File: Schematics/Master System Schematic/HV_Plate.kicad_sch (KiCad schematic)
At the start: 14 parts, among them K5 AIR-: GX14, K6 PCharge: P105BDA, K7 AIR+: GX14, K8 DCharge: PNC113, U7 OrionCurrentSens

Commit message: ESF-2 2023 Updates (#136)
* Moved shutdown loop & TSMPs

* Moved Dashboard/Footwellbox

* Deleted SSOKs

* More stuff

* Charger and battbox stuff

* Added battbox fans

* Updated sheet sizing

* Flipped MC

 to make powertrain ordering better

* Updated HV plate

* IDrk

* Better topsheet labels

* Segment Layer updates

Adding shepherd

* LV Plate update

* Partial work on accumulator container sheet

To be continued

* Finish accumulator

* Footwell updates

* Removing old files

* Added Wheel

* Top sheet budge

* Renumbered pages

* Shutdown Summary Updates

* Missed some TSV color

* Export shutdown summary

* Deleted more old files

* Added TSAL17

* Added TS-GLV17

* Added Wheel17

* Other NER lib cleanup

* Annotations

* More annotate and export

* Moved PDF

* Reexport master schem

* Cleaning out old shutdown summary files

* MATLAB!

For precharge and discharge plotting

* Changed label alignment

* Updated dashboard name

* Updated for LFP board and bigger top sheet

* backup

* Changed breaker to fuse in Shutdown Simmary

* Finished traces

* Oops forgot to merge
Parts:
- added F906: DCDC Fuse+: 5A, symbol Device:Fuse
- added F907: DCDC Fuse-: 5A, symbol Device:Fuse
- K901: renamed from K5; value AIR-: GX14 -> AIR-: GV24
- K902: renamed from K6; value PCharge: P105BDA -> PCharge: 2-1904058-5
- K903: renamed from K7; value AIR+: GX14 -> AIR+: GV24
- K904: renamed from K8; value DCharge: PNC113 -> DCharge: CPC1135N
- R901: renamed from R8; value PCharge: 600R -> PCharge: 1K
- R902: renamed from R9; value DCharge: 3.3K -> DCharge: 5K
- renumbered F190 to F901, F191 to F902, F192 to F903, F193 to F904, F194 to F905, R10 to R903, R11 to R904, U7 to U901
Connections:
- net AIR-_SigL is gone; now on net RlyCtrlGND: K901.6
- net DCharge_SigL is gone; now on net RlyCtrlGND: K904.5
- net PCharge_SigL is gone; now on net RlyCtrlGND: K902.6
- net TS+: now also F906.1
- net TS-: now also F907.1
- net AIR+_SigL renamed RlyCtrlGND
- new net DCDC_TS+: F906.2
- new net DCDC_TS-: F907.2
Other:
- note added: "SEE ALTIUM SCHEMATIC FOR FINAL IMPLEMENTATION"
- note removed: "20AWG"

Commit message: Revert "ESF-2 2023 Updates (#136)"
This reverts commit dbac7da28cdaad5f36fde89af32aad76a0b85ea3.
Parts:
- removed F906: DCDC Fuse+: 5A, symbol Device:Fuse
- removed F907: DCDC Fuse-: 5A, symbol Device:Fuse
- K5: renamed from K901; value AIR-: GV24 -> AIR-: GX14
- K6: renamed from K902; value PCharge: 2-1904058-5 -> PCharge: P105BDA
- K7: renamed from K903; value AIR+: GV24 -> AIR+: GX14
- K8: renamed from K904; value DCharge: CPC1135N -> DCharge: PNC113
- R8: renamed from R901; value PCharge: 1K -> PCharge: 600R
- R9: renamed from R902; value DCharge: 5K -> DCharge: 3.3K
- renumbered F901 to F190, F902 to F191, F903 to F192, F904 to F193, F905 to F194, R903 to R10, R904 to R11, U901 to U7
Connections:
- removed net RlyCtrlGND: K5.6, K6.6, K7.6, K8.5
- new net AIR+_SigL: K7.6
- new net AIR-_SigL: K5.6
- new net DCharge_SigL: K8.5
- new net PCharge_SigL: K6.6
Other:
- note added: "20AWG"
- note removed: "SEE ALTIUM SCHEMATIC FOR FINAL IMPLEMENTATION"

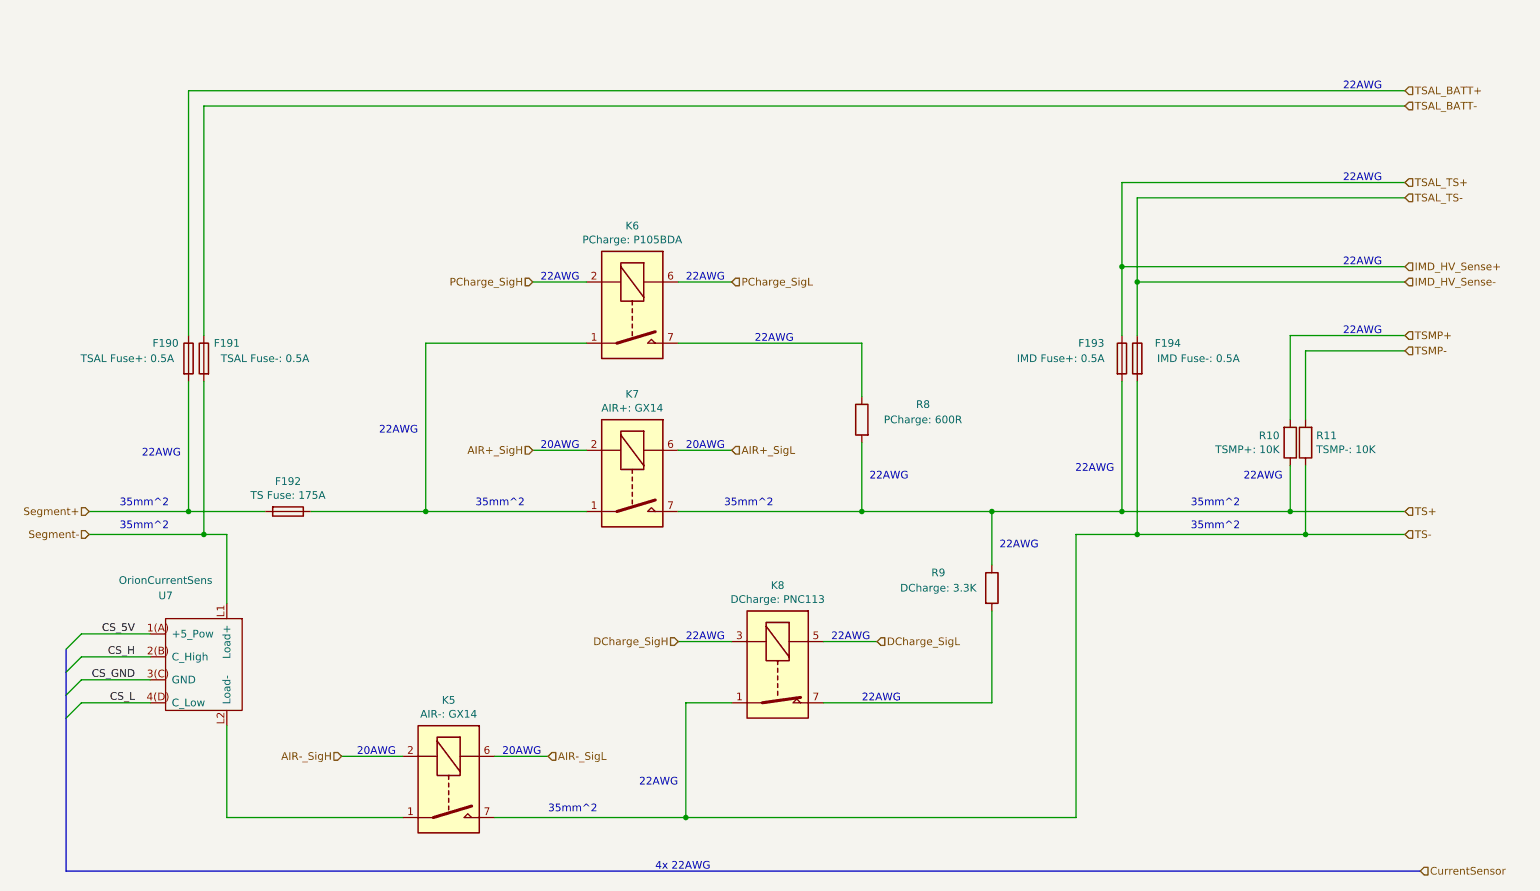
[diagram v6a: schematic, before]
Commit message: Updated HV plate
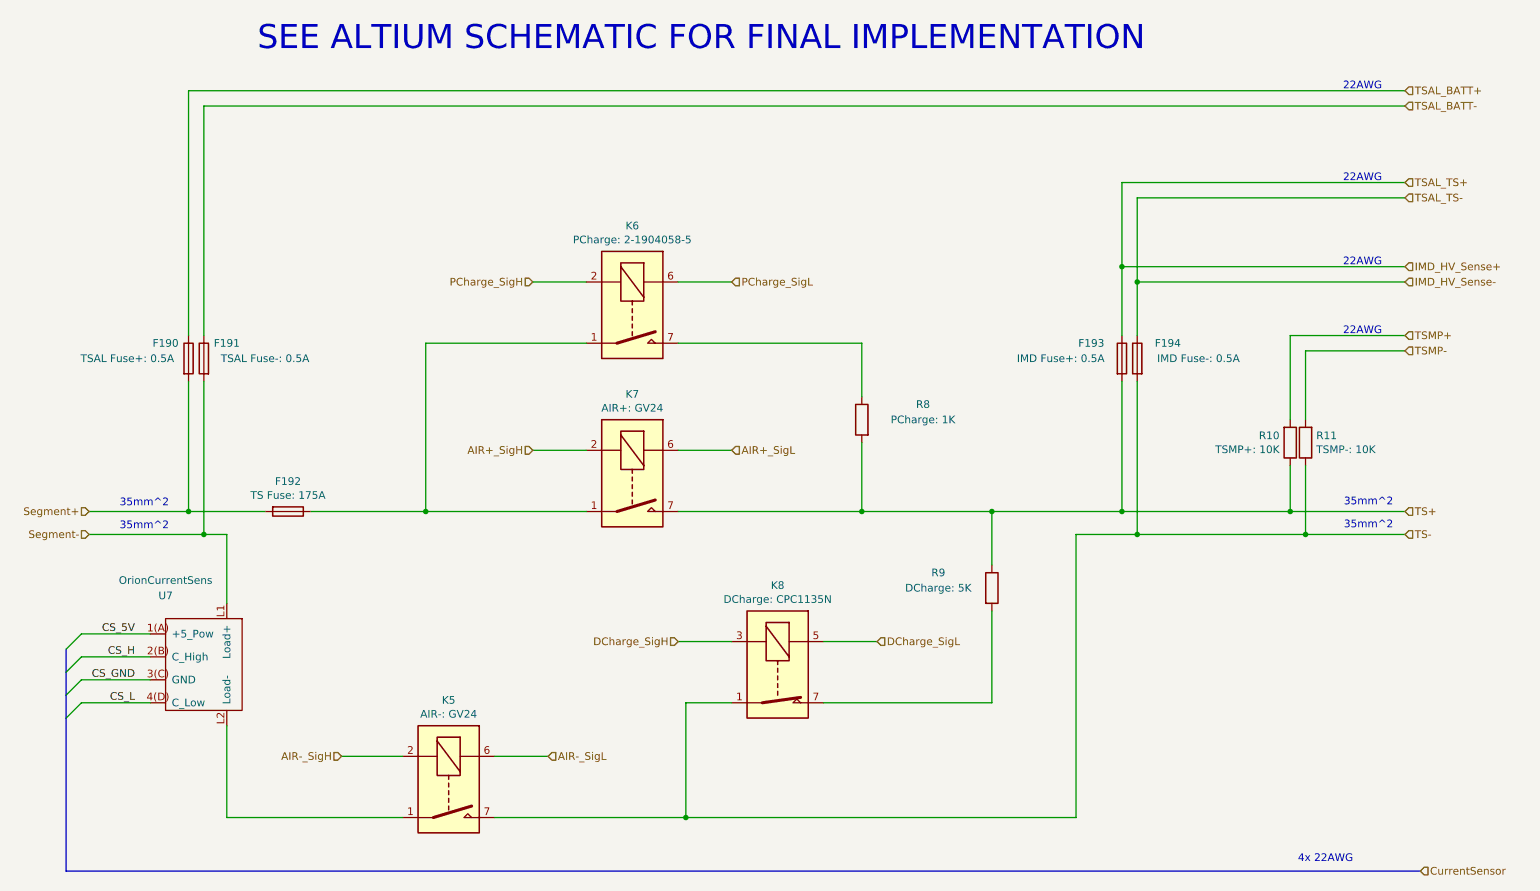
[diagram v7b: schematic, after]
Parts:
- K5: value AIR-: GX14 -> AIR-: GV24
- K6: value PCharge: P105BDA -> PCharge: 2-1904058-5
- K7: value AIR+: GX14 -> AIR+: GV24
- K8: value DCharge: PNC113 -> DCharge: CPC1135N
- R8: value PCharge: 600R -> PCharge: 1K
- R9: value DCharge: 3.3K -> DCharge: 5K
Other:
- note added: "SEE ALTIUM SCHEMATIC FOR FINAL IMPLEMENTATION"
- note removed: "20AWG"
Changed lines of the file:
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@@
   (title_block
     (title "HV Plate")
-    (date "2021-04-15")
-    (rev "1.0")
+    (date "2023-01-24")
+    (rev "2")
     (company "Northeastern Electric Racing")
     (comment 1 "https://github.com/Northeastern-Electric-Racing/NER")
@@
     (stroke (width 1) (type default) (color 221 133 0 1))
   )
-  (text "35mm^2" (at 92.075 99.695 0)
+  (text "22AWG" (at 242.57 71.12 180)
+    (effects (font (size 1.27 1.27)) (justify right bottom))
+  )
+  (text "SEE ALTIUM SCHEMATIC FOR FINAL IMPLEMENTATION" (at 55.88 24.13 0)
+    (effects (font (size 3.9878 3.9878)) (justify left bottom))
+  )
+  (text "22AWG" (at 242.57 30.48 180)
+    (effects (font (size 1.27 1.27)) (justify right bottom))
+  )
+  (text "4x 22AWG" (at 228.6 158.75 0)
     (effects (font (size 1.27 1.27)) (justify left bottom))
-  )
-  (text "22AWG" (at 179.07 106.68 0)
-    (effects (font (size 1.27 1.27)) (justify left bottom))
-  )
-  (text "22AWG" (at 151.13 121.92 0)
-    (effects (font (size 1.27 1.27)) (justify left bottom))
-  )
-  (text "22AWG" (at 127 121.92 0)
-    (effects (font (size 1.27 1.27)) (justify left bottom))
-  )
-  (text "22AWG" (at 242.57 71.12 180)
-    (effects (font (size 1.27 1.27)) (justify right bottom))
-  )
-  (text "22AWG" (at 157.48 95.25 0)
-    (effects (font (size 1.27 1.27)) (justify left bottom))
-  )
-  (text "22AWG" (at 226.06 95.25 180)
-    (effects (font (size 1.27 1.27)) (justify right bottom))
-  )
-  (text "22AWG" (at 242.57 30.48 180)
-    (effects (font (size 1.27 1.27)) (justify right bottom))
-  )
-  (text "20AWG" (at 96.52 140.97 0)
-    (effects (font (size 1.27 1.27)) (justify left bottom))
-  )
-  (text "20AWG" (at 72.39 140.97 0)
-    (effects (font (size 1.27 1.27)) (justify left bottom))
-  )
-  (text "22AWG" (at 156.21 132.08 0)
-    (effects (font (size 1.27 1.27)) (justify left bottom))
-  )
-  (text "35mm^2" (at 133.35 99.695 0)
-    (effects (font (size 1.27 1.27)) (justify left bottom))
-  )
-  (text "20AWG" (at 127 90.17 0)
-    (effects (font (size 1.27 1.27)) (justify left bottom))
-  )
-  (text "22AWG" (at 138.43 72.39 0)
-    (effects (font (size 1.27 1.27)) (justify left bottom))
-  )
-  (text "4x 22AWG" (at 121.92 160.02 0)
-    (effects (font (size 1.27 1.27)) (justify left bottom))
-  )
-  (text "22AWG" (at 125.73 146.05 180)
-    (effects (font (size 1.27 1.27)) (justify right bottom))
-  )
-  (text "22AWG" (at 82.55 87.63 180)
-    (effects (font (size 1.27 1.27)) (justify right bottom))
   )
   (text "35mm^2" (at 33.02 103.505 0)
     (effects (font (size 1.27 1.27)) (justify left bottom))
   )
-  (text "35mm^2" (at 210.82 103.505 0)
+  (text "35mm^2" (at 236.2396 103.351 0)
     (effects (font (size 1.27 1.27)) (justify left bottom))
   )
-  (text "20AWG" (at 102.87 90.17 0)
-    (effects (font (size 1.27 1.27)) (justify left bottom))
-  )
   (text "22AWG" (at 242.57 59.69 180)
     (effects (font (size 1.27 1.27)) (justify right bottom))
   )
-  (text "22AWG" (at 127 62.23 0)
-    (effects (font (size 1.27 1.27)) (justify left bottom))
-  )
   (text "22AWG" (at 242.57 45.72 180)
     (effects (font (size 1.27 1.27)) (justify right bottom))
   )
-  (text "22AWG" (at 43.18 91.44 180)
-    (effects (font (size 1.27 1.27)) (justify right bottom))
-  )
-  (text "22AWG" (at 198.12 93.98 180)
-    (effects (font (size 1.27 1.27)) (justify right bottom))
-  )
-  (text "22AWG" (at 102.87 62.23 0)
-    (effects (font (size 1.27 1.27)) (justify left bottom))
-  )
-  (text "35mm^2" (at 210.82 99.695 0)
-    (effects (font (size 1.27 1.27)) (justify left bottom))
-  )
-  (text "35mm^2" (at 104.14 150.495 0)
+  (text "35mm^2" (at 236.2396 99.541 0)
     (effects (font (size 1.27 1.27)) (justify left bottom))
   )
@@
     (in_bom yes) (on_board yes)
     (property "Reference" "R9" (id 0) (at 168.91 110.49 0))
-    (property "Value" "DCharge: 3.3K" (id 1) (at 168.91 113.03 0))
+    (property "Value" "DCharge: 5K" (id 1) (at 168.91 113.03 0))
     (property "Footprint" "" (id 2) (at 176.022 113.03 90)
       (effects (font (size 1.27 1.27)) hide)
@@
     (in_bom yes) (on_board yes)
     (property "Reference" "R8" (id 0) (at 166.37 82.55 0))
-    (property "Value" "PCharge: 600R" (id 1) (at 166.37 85.09 0))
+    (property "Value" "PCharge: 1K" (id 1) (at 166.37 85.09 0))
     (property "Footprint" "" (id 2) (at 157.988 85.09 90)
       (effects (font (size 1.27 1.27)) hide)
@@
     (in_bom yes) (on_board yes)
     (property "Reference" "K5" (id 0) (at 87.63 131.6482 90))
-    (property "Value" "AIR-: GX14" (id 1) (at 87.63 133.9596 90))
+    (property "Value" "AIR-: GV24" (id 1) (at 87.63 133.9596 90))
     (property "Footprint" "Relay_THT:Relay_StandexMeder_DIP_LowProfile" (id 2) (at 86.36 154.94 0)
       (effects (font (size 1.27 1.27)) (justify left) hide)
@@
     (in_bom yes) (on_board yes)
     (property "Reference" "K6" (id 0) (at 118.11 52.9082 90))
-    (property "Value" "PCharge: P105BDA" (id 1) (at 118.11 55.2196 90))
+    (property "Value" "PCharge: 2-1904058-5" (id 1) (at 118.11 55.2196 90))
     (property "Footprint" "Relay_THT:Relay_StandexMeder_DIP_LowProfile" (id 2) (at 116.84 76.2 0)
       (effects (font (size 1.27 1.27)) (justify left) hide)
@@
     (in_bom yes) (on_board yes)
     (property "Reference" "K7" (id 0) (at 118.11 80.8482 90))
-    (property "Value" "AIR+: GX14" (id 1) (at 118.11 83.1596 90))
+    (property "Value" "AIR+: GV24" (id 1) (at 118.11 83.1596 90))
     (property "Footprint" "Relay_THT:Relay_StandexMeder_DIP_LowProfile" (id 2) (at 116.84 104.14 0)
       (effects (font (size 1.27 1.27)) (justify left) hide)
@@
     (in_bom yes) (on_board yes)
     (property "Reference" "K8" (id 0) (at 142.24 112.5982 90))
-    (property "Value" "DCharge: PNC113" (id 1) (at 142.24 114.9096 90))
+    (property "Value" "DCharge: CPC1135N" (id 1) (at 142.24 114.9096 90))
     (property "Footprint" "Relay_THT:Relay_SPST_StandexMeder_MS_Form1AB" (id 2) (at 140.97 135.89 0)
       (effects (font (size 1.27 1.27)) (justify left) hide)

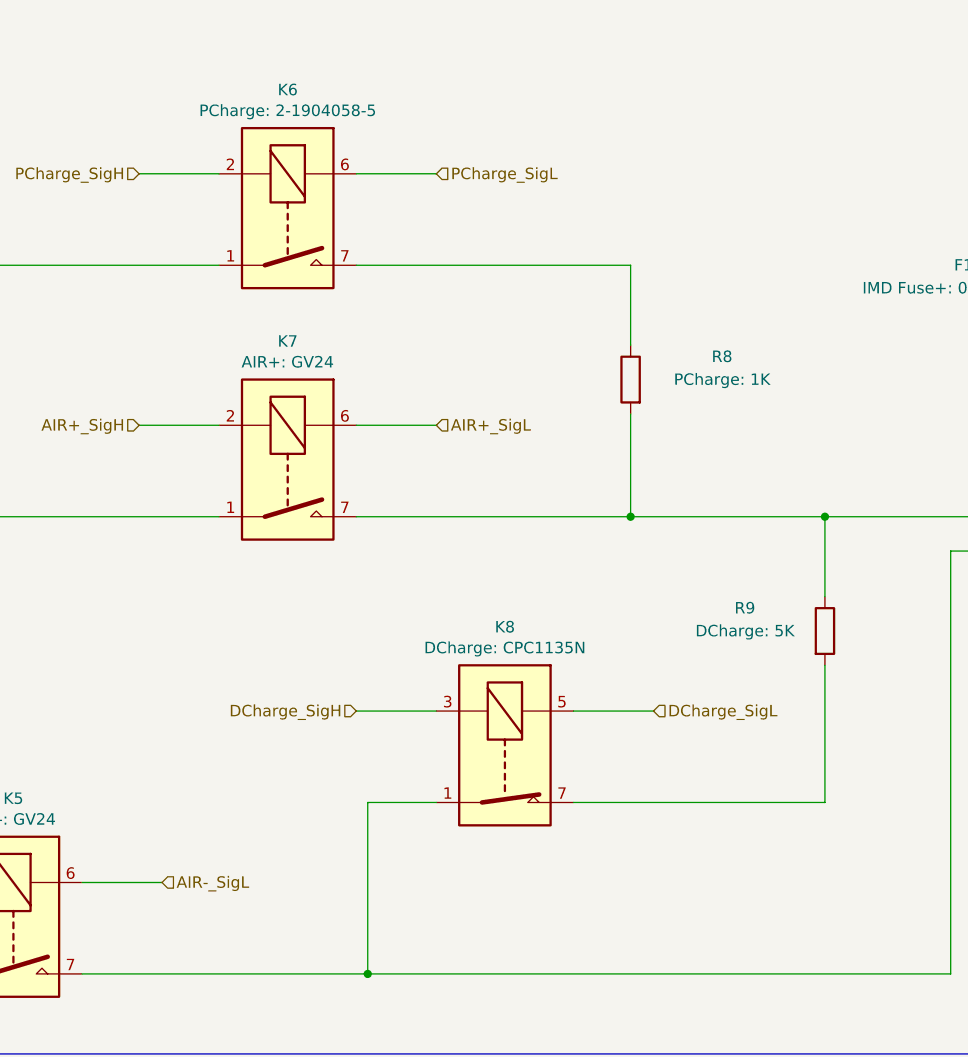
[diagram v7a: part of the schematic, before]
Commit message: Partial work on accumulator container sheet
To be continued
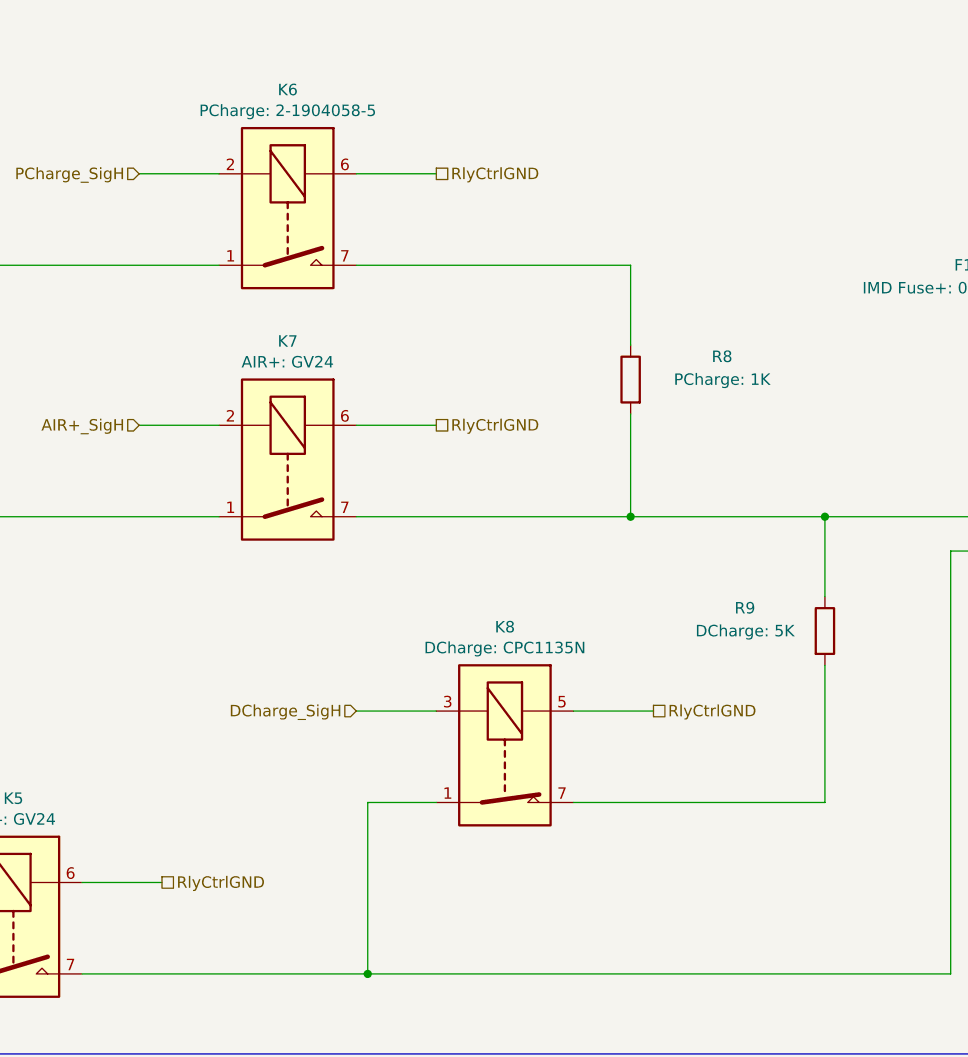
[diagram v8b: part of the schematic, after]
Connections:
- net AIR-_SigL is gone; now on net RlyCtrlGND: K5.6
- net DCharge_SigL is gone; now on net RlyCtrlGND: K8.5
- net PCharge_SigL is gone; now on net RlyCtrlGND: K6.6
- net AIR+_SigL renamed RlyCtrlGND
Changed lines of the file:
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@@
+    (effects (font (size 1.27 1.27)) (justify left))
+  )
+  (hierarchical_label "RlyCtrlGND" (shape passive) (at 158.75 121.92 0)
     (effects (font (size 1.27 1.27)) (justify left))
   )
@@
   (hierarchical_label "DCharge_SigH" (shape input) (at 125.73 121.92 180)
     (effects (font (size 1.27 1.27)) (justify right))
+  )
+  (hierarchical_label "RlyCtrlGND" (shape passive) (at 134.62 90.17 0)
+    (effects (font (size 1.27 1.27)) (justify left))
   )
   (hierarchical_label "TSAL_TS+" (shape input) (at 246.38 45.72 0)
@@
     (effects (font (size 1.27 1.27)) (justify left))
   )
-  (hierarchical_label "AIR+_SigL" (shape input) (at 134.62 90.17 0)
-    (effects (font (size 1.27 1.27)) (justify left))
-  )
   (hierarchical_label "Segment+" (shape input) (at 27.94 100.33 180)
     (effects (font (size 1.27 1.27)) (justify right))
   )
-  (hierarchical_label "DCharge_SigL" (shape input) (at 158.75 121.92 0)
+  (hierarchical_label "RlyCtrlGND" (shape passive) (at 104.14 140.97 0)
     (effects (font (size 1.27 1.27)) (justify left))
   )
-  (hierarchical_label "PCharge_SigL" (shape input) (at 134.62 62.23 0)
+  (hierarchical_label "RlyCtrlGND" (shape passive) (at 134.62 62.23 0)
     (effects (font (size 1.27 1.27)) (justify left))
   )
-  (hierarchical_label "AIR-_SigL" (shape input) (at 104.14 140.97 0)
-    (effects (font (size 1.27 1.27)) (justify left))
-  )
